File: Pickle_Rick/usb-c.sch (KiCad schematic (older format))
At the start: 5 parts, among them J1 USB_C_Receptacle_USB2.0

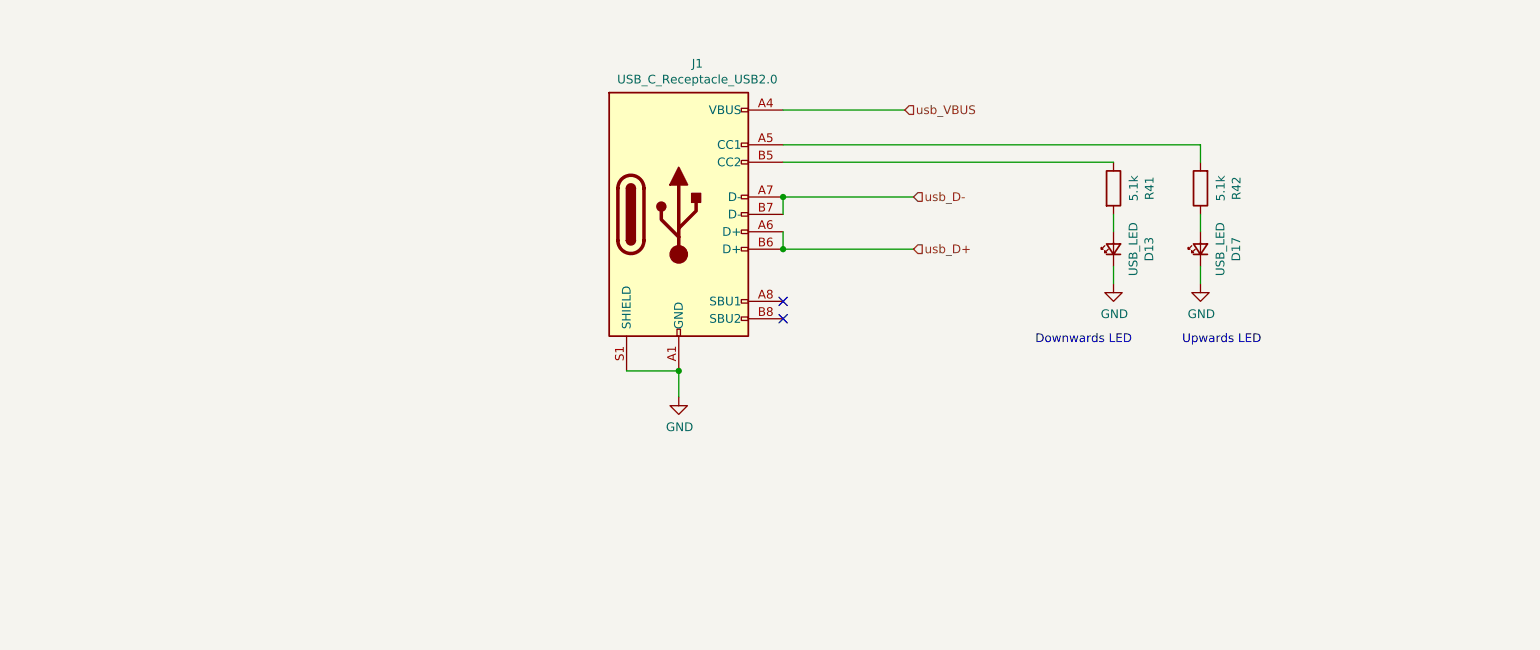
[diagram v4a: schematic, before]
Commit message: changed usb 2.0 to 3.0; started pcb design; changed flash symbol
need to change flash footprint still
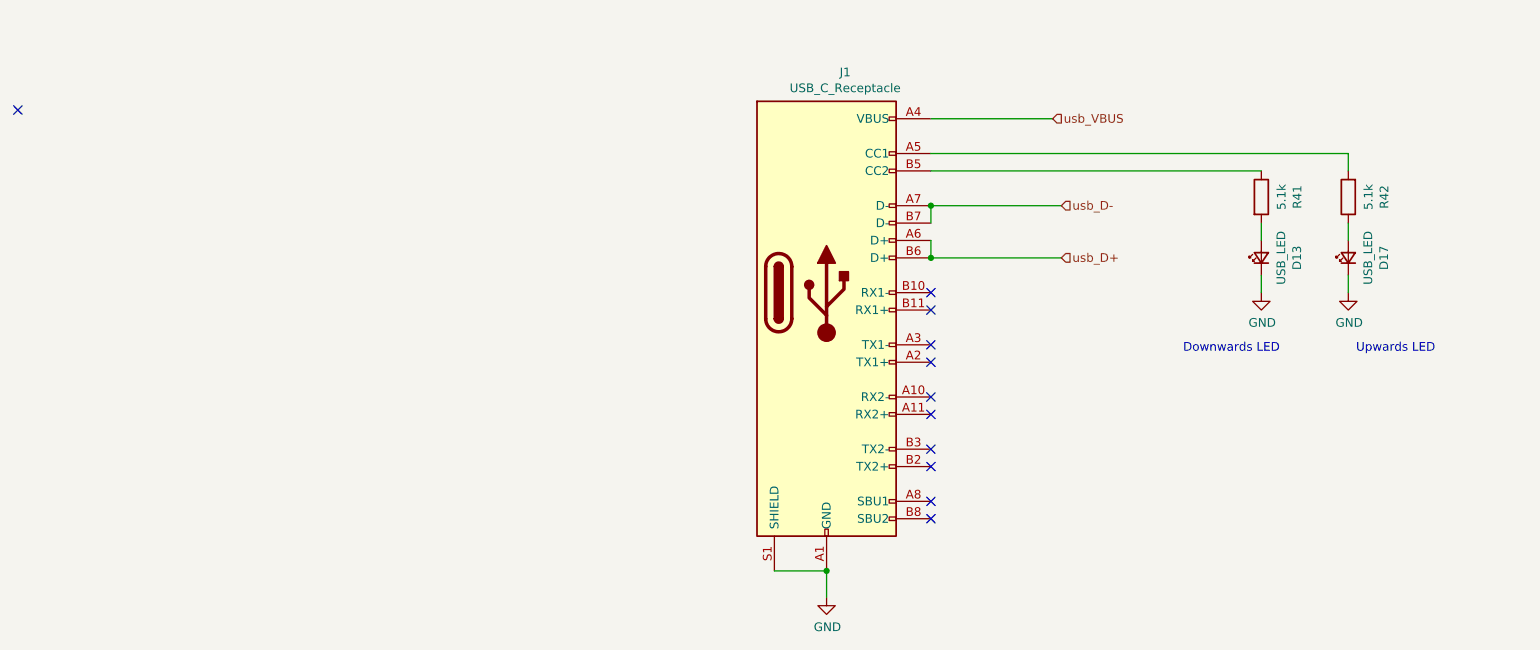
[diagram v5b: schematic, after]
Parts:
- removed J1: USB_C_Receptacle_USB2.0, symbol Connector:USB_C_Receptacle_USB2.0
- added J1: USB_C_Receptacle, Connector_USB:USB_C_Receptacle_Amphenol_12401548E4-2A, symbol Connector:USB_C_Receptacle
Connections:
- net GND: now also J1.A1 (GND), J1.A12 (GND), J1.B1 (GND), J1.B12 (GND), J1.S1 (SHIELD)
- net usb_D+: now also J1.A6 (D+), J1.B6 (D+)
- net usb_D-: now also J1.A7 (D-), J1.B7 (D-)
- net usb_VBUS: now also J1.A4 (VBUS), J1.A9 (VBUS), J1.B4 (VBUS), J1.B9 (VBUS)
- net at R42.2: now also J1.A5 (CC1)
- net at R41.1: now also J1.B5 (CC2)
- no-connect marks 2 -> 11
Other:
- moved on the sheet: D13, D17, R41, R42
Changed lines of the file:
@@
 Comment4 ""
 $EndDescr
-Text HLabel 5450 3500 2    50   Input ~ 0
-usb_D+
-Text HLabel 5450 3200 2    50   Input ~ 0
-usb_D-
-Text HLabel 5400 2700 2    50   Input ~ 0
-usb_VBUS
+$Comp
+L Device:R R42
+U 1 1 6043A0B1
+P 7950 3200
+F 0 "R42" V 7743 3200 50  0000 C CNN
+F 1 "5.1k" V 7834 3200 50  0000 C CNN
+F 2 "Resistor_SMD:R_0603_1608Metric" V 7880 3200 50  0001 C CNN
+F 3 "~" H 7950 3200 50  0001 C CNN
+	1    7950 3200
+	-1   0    0    1
+$EndComp
 Wire Wire Line
-	4700 3200 4700 3300
-Wire Wire Line
-	4700 3200 5450 3200
-Wire Wire Line
-	4700 3400 4700 3500
-Wire Wire Line
-	5450 3500 4700 3500
+	7950 2950 7950 3050
 $Comp
-L power:GND #PWR0110
-U 1 1 60735E2B
-P 4100 4350
-F 0 "#PWR0110" H 4100 4100 50  0001 C CNN
-F 1 "GND" H 4105 4177 50  0000 C CNN
-F 2 "" H 4100 4350 50  0001 C CNN
-F 3 "" H 4100 4350 50  0001 C CNN
-	1    4100 4350
+L Device:R R41
+U 1 1 6043AE1B
+P 7450 3200
+F 0 "R41" V 7657 3200 50  0000 C CNN
+F 1 "5.1k" V 7566 3200 50  0000 C CNN
+F 2 "Resistor_SMD:R_0603_1608Metric" V 7380 3200 50  0001 C CNN
+F 3 "~" H 7450 3200 50  0001 C CNN
+	1    7450 3200
 	1    0    0    -1
 $EndComp
 Wire Wire Line
-	4100 4350 4100 4200
-NoConn ~ 4700 3800
-NoConn ~ 4700 3900
-Connection ~ 4100 4200
-Connection ~ 4700 3200
-Connection ~ 4700 3500
+	5550 2950 7950 2950
 Wire Wire Line
-	3800 4200 4100 4200
-$Comp
-L Connector:USB_C_Receptacle_USB2.0 J1
-U 1 1 607282EC
-P 4100 3300
-F 0 "J1" H 4207 4167 50  0000 C CNN
-F 1 "USB_C_Receptacle_USB2.0" H 4207 4076 50  0000 C CNN
-F 2 "" H 4250 3300 50  0001 C CNN
-F 3 "https://www.usb.org/sites/default/files/documents/usb_type-c.zip" H 4250 3300 50  0001 C CNN
-	1    4100 3300
-	1    0    0    -1
-$EndComp
-$Comp
-L Device:R R42
-U 1 1 6043A0B1
-P 7100 3150
-F 0 "R42" V 6893 3150 50  0000 C CNN
-F 1 "5.1k" V 6984 3150 50  0000 C CNN
-F 2 "Resistor_SMD:R_0603_1608Metric" V 7030 3150 50  0001 C CNN
-F 3 "~" H 7100 3150 50  0001 C CNN
-	1    7100 3150
-	-1   0    0    1
-$EndComp
-Wire Wire Line
-	7100 2900 7100 3000
-Wire Wire Line
-	4700 2700 5400 2700
-$Comp
-L Device:R R41
-U 1 1 6043AE1B
-P 6600 3150
-F 0 "R41" V 6807 3150 50  0000 C CNN
-F 1 "5.1k" V 6716 3150 50  0000 C CNN
-F 2 "Resistor_SMD:R_0603_1608Metric" V 6530 3150 50  0001 C CNN
-F 3 "~" H 6600 3150 50  0001 C CNN
-	1    6600 3150
-	1    0    0    -1
-$EndComp
-Wire Wire Line
-	4700 2900 7100 2900
-Wire Wire Line
-	4700 3000 6600 3000
+	5550 3050 7450 3050
 $Comp
 L power:GND #PWR01
 U 1 1 60488D63
-P 6600 3700
-F 0 "#PWR01" H 6600 3450 50  0001 C CNN
-F 1 "GND" H 6605 3527 50  0000 C CNN
-F 2 "" H 6600 3700 50  0001 C CNN
-F 3 "" H 6600 3700 50  0001 C CNN
-	1    6600 3700
+P 7450 3750
+F 0 "#PWR01" H 7450 3500 50  0001 C CNN
+F 1 "GND" H 7455 3577 50  0000 C CNN
+F 2 "" H 7450 3750 50  0001 C CNN
+F 3 "" H 7450 3750 50  0001 C CNN
+	1    7450 3750
 	1    0    0    -1
 $EndComp
@@
 L power:GND #PWR055
 U 1 1 60489008
-P 7100 3700
-F 0 "#PWR055" H 7100 3450 50  0001 C CNN
-F 1 "GND" H 7105 3527 50  0000 C CNN
-F 2 "" H 7100 3700 50  0001 C CNN
-F 3 "" H 7100 3700 50  0001 C CNN
-	1    7100 3700
+P 7950 3750
+F 0 "#PWR055" H 7950 3500 50  0001 C CNN
+F 1 "GND" H 7955 3577 50  0000 C CNN
+F 2 "" H 7950 3750 50  0001 C CNN
+F 3 "" H 7950 3750 50  0001 C CNN
+	1    7950 3750
 	1    0    0    -1
 $EndComp
@@
 L Device:LED_Small D?
 U 1 1 6053D295
-P 6600 3500
+P 7450 3550
 AR Path="/6053D295" Ref="D?"  Part="1"
 AR Path="/602F075A/6053D295" Ref="D13"  Part="1"
-F 0 "D13" H 6600 3295 50  0000 C CNN
-F 1 "USB_LED" H 6600 3386 50  0000 C CNN
-F 2 "LED_SMD:LED_0603_1608Metric_Castellated" V 6600 3500 50  0001 C CNN
-F 3 "~" V 6600 3500 50  0001 C CNN
-	1    6600 3500
+F 0 "D13" H 7450 3345 50  0000 C CNN
+F 1 "USB_LED" H 7450 3436 50  0000 C CNN
+F 2 "LED_SMD:LED_0603_1608Metric_Castellated" V 7450 3550 50  0001 C CNN
+F 3 "~" V 7450 3550 50  0001 C CNN
+	1    7450 3550
 	0    -1   -1   0
 $EndComp
 Wire Wire Line
-	6600 3300 6600 3400
+	7450 3350 7450 3450
 Wire Wire Line
-	6600 3600 6600 3700
+	7450 3650 7450 3750
 Wire Wire Line
-	7100 3700 7100 3600
+	7950 3750 7950 3650
 $Comp
 L Device:LED_Small D?
 U 1 1 604A9E91
-P 7100 3500
+P 7950 3550
 AR Path="/604A9E91" Ref="D?"  Part="1"
 AR Path="/602F075A/604A9E91" Ref="D17"  Part="1"
-F 0 "D17" H 7100 3295 50  0000 C CNN
-F 1 "USB_LED" H 7100 3386 50  0000 C CNN
-F 2 "LED_SMD:LED_0603_1608Metric_Castellated" V 7100 3500 50  0001 C CNN
-F 3 "~" V 7100 3500 50  0001 C CNN
-	1    7100 3500
+F 0 "D17" H 7950 3345 50  0000 C CNN
+F 1 "USB_LED" H 7950 3436 50  0000 C CNN
+F 2 "LED_SMD:LED_0603_1608Metric_Castellated" V 7950 3550 50  0001 C CNN
+F 3 "~" V 7950 3550 50  0001 C CNN
+	1    7950 3550
 	0    -1   -1   0
 $EndComp
 Wire Wire Line
-	7100 3400 7100 3300
-Text Notes 7450 4050 2    50   ~ 0
+	7950 3450 7950 3350
+Text Notes 8450 4100 2    50   ~ 0
 Upwards LED
-Text Notes 6150 4050 0    50   ~ 0
+Text Notes 7000 4100 0    50   ~ 0
 Downwards LED
+$Comp
+L Connector:USB_C_Receptacle J1
+U 1 1 604B4652
+P 4950 3750
+F 0 "J1" H 5057 5017 50  0000 C CNN
+F 1 "USB_C_Receptacle" H 5057 4926 50  0000 C CNN
+F 2 "Connector_USB:USB_C_Receptacle_Amphenol_12401548E4-2A" H 5100 3750 50  0001 C CNN
+F 3 "https://www.usb.org/sites/default/files/documents/usb_type-c.zip" H 5100 3750 50  0001 C CNN
+	1    4950 3750
+	1    0    0    -1
+$EndComp
+Wire Wire Line
+	4650 5350 4950 5350
+Wire Wire Line
+	4950 5500 4950 5350
+$Comp
+L power:GND #PWR0110
+U 1 1 60735E2B
+P 4950 5500
+F 0 "#PWR0110" H 4950 5250 50  0001 C CNN
+F 1 "GND" H 4955 5327 50  0000 C CNN
+F 2 "" H 4950 5500 50  0001 C CNN
+F 3 "" H 4950 5500 50  0001 C CNN
+	1    4950 5500
+	1    0    0    -1
+$EndComp
+Connection ~ 4950 5350
+Wire Wire Line
+	5550 2750 6250 2750
+Text HLabel 6250 2750 2    50   Input ~ 0
+usb_VBUS
+Wire Wire Line
+	6300 3550 5550 3550
+Wire Wire Line
+	5550 3250 6300 3250
+Text HLabel 6300 3250 2    50   Input ~ 0
+usb_D-
+Text HLabel 6300 3550 2    50   Input ~ 0
+usb_D+
+Wire Wire Line
+	5550 3350 5550 3250
+Connection ~ 5550 3250
+Wire Wire Line
+	5550 3450 5550 3550
+Connection ~ 5550 3550
+NoConn ~ 5550 3750
+NoConn ~ 5550 3850
+NoConn ~ 5550 4050
+NoConn ~ 5550 4150
+NoConn ~ 5550 4350
+NoConn ~ 5550 4450
+NoConn ~ 5550 4650
+NoConn ~ 5550 4750
+NoConn ~ 5550 4950
+NoConn ~ 5550 5050
+NoConn ~ 300  2700
 $EndSCHEMATC

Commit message: did some pcb thing
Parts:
- D13: value USB_LED -> down_led
- D17: value USB_LED -> up_led
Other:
- note removed: "Downwards LED"
- note removed: "Upwards LED"
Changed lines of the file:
@@
 $Descr A4 11693 8268
 encoding utf-8
-Sheet 7 7
+Sheet 5 7
 Title ""
 Date ""
@@
 	1    0    0    -1
 $EndComp
-$Comp
-L Device:LED_Small D?
-U 1 1 6053D295
-P 7450 3550
-AR Path="/6053D295" Ref="D?"  Part="1"
-AR Path="/602F075A/6053D295" Ref="D13"  Part="1"
-F 0 "D13" H 7450 3345 50  0000 C CNN
-F 1 "USB_LED" H 7450 3436 50  0000 C CNN
-F 2 "LED_SMD:LED_0603_1608Metric_Castellated" V 7450 3550 50  0001 C CNN
-F 3 "~" V 7450 3550 50  0001 C CNN
-	1    7450 3550
-	0    -1   -1   0
-$EndComp
 Wire Wire Line
 	7450 3350 7450 3450
@@
 AR Path="/602F075A/604A9E91" Ref="D17"  Part="1"
 F 0 "D17" H 7950 3345 50  0000 C CNN
-F 1 "USB_LED" H 7950 3436 50  0000 C CNN
+F 1 "up_led" H 7950 3436 50  0000 C CNN
 F 2 "LED_SMD:LED_0603_1608Metric_Castellated" V 7950 3550 50  0001 C CNN
 F 3 "~" V 7950 3550 50  0001 C CNN
@@
 Wire Wire Line
 	7950 3450 7950 3350
-Text Notes 8450 4100 2    50   ~ 0
-Upwards LED
-Text Notes 7000 4100 0    50   ~ 0
-Downwards LED
 $Comp
 L Connector:USB_C_Receptacle J1
@@
 NoConn ~ 5550 5050
 NoConn ~ 300  2700
+$Comp
+L Device:LED_Small D?
+U 1 1 6053D295
+P 7450 3550
+AR Path="/6053D295" Ref="D?"  Part="1"
+AR Path="/602F075A/6053D295" Ref="D13"  Part="1"
+F 0 "D13" H 7450 3345 50  0000 C CNN
+F 1 "down_led" H 7450 3436 50  0000 C CNN
+F 2 "LED_SMD:LED_0603_1608Metric_Castellated" V 7450 3550 50  0001 C CNN
+F 3 "~" V 7450 3550 50  0001 C CNN
+	1    7450 3550
+	0    -1   -1   0
+$EndComp
 $EndSCHEMATC
